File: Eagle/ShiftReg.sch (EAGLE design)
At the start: 194 parts, among them Q100 310mA/60V/1.6Ω, Q101 310mA/60V/1.6Ω, Q102 310mA/60V/1.6Ω, Q103 310mA/60V/1.6Ω, Q104 310mA/60V/1.6Ω, Q105 310mA/60V/1.6Ω, Q106 310mA/60V/1.6Ω, Q107 310mA/60V/1.6Ω, Q108 310mA/60V/1.6Ω, Q109 310mA/60V/1.6Ω, Q110 310mA/60V/1.6Ω, Q111 310mA/60V/1.6Ω, Q112 310mA/60V/1.6Ω, Q113 310mA/60V/1.6Ω, Q114 310mA/60V/1.6Ω, Q115 310mA/60V/1.6Ω, Q116 310mA/60V/1.6Ω, Q117 310mA/60V/1.6Ω, Q118 310mA/60V/1.6Ω, Q119 310mA/60V/1.6Ω, Q120 310mA/60V/1.6Ω, Q121 310mA/60V/1.6Ω, Q122 310mA/60V/1.6Ω, Q123 310mA/60V/1.6Ω, Q124 310mA/60V/1.6Ω, Q125 310mA/60V/1.6Ω, Q126 310mA/60V/1.6Ω, Q127 310mA/60V/1.6Ω, Q128 310mA/60V/1.6Ω, Q129 310mA/60V/1.6Ω, Q130 310mA/60V/1.6Ω, Q131 310mA/60V/1.6Ω, Q132 310mA/60V/1.6Ω, Q166 310mA/60V/1.6Ω, Q167 310mA/60V/1.6Ω, Q168 310mA/60V/1.6Ω, Q169 310mA/60V/1.6Ω, Q170 310mA/60V/1.6Ω, Q171 310mA/60V/1.6Ω, Q172 310mA/60V/1.6Ω, Q173 310mA/60V/1.6Ω, Q174 310mA/60V/1.6Ω, Q175 310mA/60V/1.6Ω, Q176 310mA/60V/1.6Ω, Q177 310mA/60V/1.6Ω, Q178 310mA/60V/1.6Ω, Q179 310mA/60V/1.6Ω, Q180 310mA/60V/1.6Ω, Q181 310mA/60V/1.6Ω, Q182 310mA/60V/1.6Ω, Q183 310mA/60V/1.6Ω, Q184 310mA/60V/1.6Ω, Q185 310mA/60V/1.6Ω, Q186 310mA/60V/1.6Ω, Q187 310mA/60V/1.6Ω, Q188 310mA/60V/1.6Ω, Q189 310mA/60V/1.6Ω, Q190 310mA/60V/1.6Ω, Q191 310mA/60V/1.6Ω, Q192 310mA/60V/1.6Ω, Q193 310mA/60V/1.6Ω, Q194 310mA/60V/1.6Ω, Q195 310mA/60V/1.6Ω, Q196 310mA/60V/1.6Ω, Q197 310mA/60V/1.6Ω, Q198 310mA/60V/1.6Ω, Q232 310mA/60V/1.6Ω, Q233 310mA/60V/1.6Ω, Q234 310mA/60V/1.6Ω, Q235 310mA/60V/1.6Ω, Q236 310mA/60V/1.6Ω, Q237 310mA/60V/1.6Ω, Q238 310mA/60V/1.6Ω, Q239 310mA/60V/1.6Ω, Q240 310mA/60V/1.6Ω, Q241 310mA/60V/1.6Ω, Q242 310mA/60V/1.6Ω, Q243 310mA/60V/1.6Ω, Q244 310mA/60V/1.6Ω, Q245 310mA/60V/1.6Ω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

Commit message: Rerouted for SOT23
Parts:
- removed Q166, Q167, Q168, Q169, Q170, Q171, Q172, Q173, Q174, Q175, Q176, Q177, Q178, Q179, Q180, Q181, Q182, Q183, Q184, Q185, Q186, Q187, Q188, Q189, Q190, Q191, Q192, Q193, Q194, Q195, Q196, Q197, Q198, Q232, Q233, Q234, Q235, Q236, Q237, Q238, Q239, Q240, Q241, Q242, Q243, Q244, Q245, Q246, Q247, Q248, Q249, Q250, Q251, Q252, Q253, Q254, Q255, Q256, Q257, Q258, Q259, Q260, Q261, Q262, Q263, Q264, Q42, Q43, Q44, Q45, Q46, Q47, Q48, Q49, Q58, Q59, Q60, Q61, Q62, Q63, Q64, Q65: 310mA/60V/1.6Ω, SparkFun-DiscreteSemi:MOSFET-NCH-2N7002PW
- removed R100, R101, R102, R103, R104, R105, R106, R107, R108, R109, R110, R111, R112, R19, R20, R21, R22, R27, R28, R71, R72, R73, R74, R75, R76, R77, R78, R79, R80, R81, R82, R83, R84, R99: (no value), SparkFun-Resistors:RESISTOR0805
- added LED1, LED2, LED3, LED4: (no value), led:LEDSQR2X5
- added Q1, Q2, Q3, Q4: (no value), XSNOR:NMOSREFLOW
- added Q10, Q11, Q12, Q13, Q133, Q134, Q135, Q136, Q137, Q138, Q139, Q14, Q140, Q141, Q142, Q143, Q144, Q145, Q146, Q147, Q148, Q149, Q15, Q150, Q151, Q152, Q153, Q154, Q155, Q156, Q157, Q158, Q159, Q16, Q160, Q161, Q162, Q163, Q164, Q165, Q25, Q26, Q27, Q28, Q29, Q30, Q31, Q32, Q67, Q68, Q69, Q70, Q71, Q72, Q73, Q74, Q75, Q76, Q77, Q78, Q79, Q80, Q81, Q82, Q83, Q84, Q85, Q86, Q87, Q88, Q89, Q9, Q90, Q91, Q92, Q93, Q94, Q95, Q96, Q97, Q98, Q99: 310mA/60V/1.6Ω, XSNOR:NMOSREFLOW
- added R1, R13, R14, R15, R16, R2, R3, R31, R32, R33, R34, R35, R36, R37, R38, R39, R4, R40, R41, R42, R5, R57, R58, R59, R6, R60, R61, R62, R63, R64, R65, R66, R67, R68, R69, R7, R70, R8: (no value), XSNOR:RESISTOR0805
- Q100, Q107, Q108, Q115, Q34, Q41: device SparkFun-DiscreteSemi:MOSFET-NCH-2N7002PW -> XSNOR:NMOSREFLOW; SPICEPREFIX M -> (none)
- Q101, Q102, Q103, Q104, Q105, Q106, Q109, Q110, Q111, Q112, Q113, Q114, Q116, Q118, Q119, Q120, Q121, Q122, Q123, Q126, Q127, Q128, Q129, Q130, Q131, Q36, Q37, Q38, Q39, Q40, Q52, Q53, Q54, Q55, Q56, Q57: device SparkFun-DiscreteSemi:MOSFET-NCH-2N7002PW -> XSNOR:NMOSREFLOW
- Q117, Q124, Q125, Q132, Q35, Q50, Q51, Q66: device SparkFun-DiscreteSemi:MOSFET-NCH-2N7002PW -> XSNOR:NMOSREFLOW; SPICEPREFIX (none) -> M
- R11, R12, R17, R18, R23, R24, R25, R26, R43, R44, R45, R46, R47, R48, R49, R50, R51, R52, R53, R54, R55, R56: device SparkFun-Resistors:RESISTOR0805 -> XSNOR:RESISTOR0805
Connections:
- removed net /Q0A1: Q36.G, Q39.D, Q40.D, Q46.G, R18.1
- removed net /Q0B: Q44.G, Q47.D, Q48.D, R22.1
- removed net /Q1A3: Q102.G, Q105.D, Q106.D, Q112.G, R46.1
- removed net /Q1B: Q110.G, Q113.D, Q114.D, R50.1
- removed net /Q2A5: Q168.G, Q171.D, Q172.D, Q178.G, R74.1
- removed net /Q2B: Q176.G, Q179.D, Q180.D, R78.1
- removed net /Q3A7: Q234.G, Q237.D, Q238.D, Q244.G, R102.1
- removed net /Q3B: Q242.G, Q245.D, Q246.D, R106.1
- removed net AUX1A': Q120.G, Q130.D, Q131.D, Q132.D, R56.2
- removed net LOAD1A': Q119.G, Q127.D, Q128.D, Q129.D, R55.2
- removed net N$116: Q243.D, Q244.D, Q245.G, R105.1
- removed net N$3: JP2.28
- removed net N$49: Q100.D, Q101.D, Q107.G, R43.1
- removed net N$50: Q103.D, Q104.D, Q105.G, R45.1
- removed net N$51: Q108.D, Q109.D, Q115.G, R47.1
- removed net N$52: Q111.D, Q112.D, Q113.G, R49.1
- removed net N$81: Q166.D, Q167.D, Q173.G, R71.1
- removed net N$82: Q169.D, Q170.D, Q171.G, R73.1
- removed net N$83: Q174.D, Q175.D, Q181.G, R75.1
- removed net N$84: Q177.D, Q178.D, Q179.G, R77.1
- removed net Q0A1: Q36.D, Q40.G, Q41.D, Q43.G, R12.1
- removed net Q1A3: Q102.D, Q106.G, Q107.D, Q109.G, R44.1
- removed net Q2A5: Q168.D, Q172.G, Q173.D, Q175.G, R72.1
- removed net Q3A7: Q234.D, Q238.G, Q239.D, Q241.G, R100.1
- removed net R0A: Q38.G, Q50.D, R23.2
- removed net S0A: Q35.G, Q50.G, Q51.D, Q52.D, Q53.D, Q54.D, R24.2
- new net AUX1A'-: Q71.G, Q81.D, Q82.D, Q83.D, R34.2
- new net LED+: JP2.28, LED1.A, LED2.A, LED3.A, LED4.A
- new net LOAD1A'-: Q70.G, Q78.D, Q79.D, Q80.D, R33.2
- new net N$10: Q92.D, Q93.D, Q99.G, R39.1
- new net N$100: Q119.D, Q123.G, Q124.D, Q126.G, R50.1
- new net N$101: Q119.G, Q122.D, Q123.D, Q129.G, R52.1
- new net N$102: Q127.G, Q130.D, Q131.D, R56.1
- new net N$103: Q86.G, Q89.D, Q90.D, Q96.G, R38.1
- new net N$104: Q86.D, Q90.G, Q91.D, Q93.G, R36.1
- new net N$105: Q94.G, Q97.D, Q98.D, R42.1
- new net N$11: Q95.D, Q96.D, Q97.G, R41.1
- new net N$110: Q53.G, Q56.D, Q57.D, R24.1
- new net N$111: Q37.G, Q40.D, Q41.D, Q55.G, R16.1
- new net N$112: Q37.D, Q41.G, Q50.D, Q52.G, R14.1
- new net N$12: Q150.D, Q151.D, Q157.G, R63.1
- new net N$13: Q153.D, Q154.D, Q155.G, R65.1
- new net N$14: Q158.D, Q159.D, Q165.G, R67.1
- new net N$15: Q161.D, Q162.D, Q163.G, R69.1
- new net N$16: Q117.D, Q118.D, Q124.G, R49.1
- new net N$17: Q120.D, Q121.D, Q122.G, R51.1
- new net N$18: Q125.D, Q126.D, Q132.G, R53.1
- new net N$19: Q128.D, Q129.D, Q130.G, R55.1
- new net N$2: Q38.D, Q39.D, Q40.G, R15.1
- new net N$20: Q3.D, R3.1
- new net N$21: Q4.D, R4.1
- new net N$22: LED4.C, R4.2
- new net N$23: LED3.C, R3.2
- new net N$24: LED2.C, R2.2
- new net N$25: LED1.C, R1.2
- new net N$7: Q54.D, Q55.D, Q56.G, R23.1
- new net N$8: Q84.D, Q85.D, Q91.G, R35.1
- new net N$9: Q87.D, Q88.D, Q89.G, R37.1
- new net R0A-: Q100.D, Q121.G, R43.2
- new net S0A-: Q100.G, Q101.D, Q102.D, Q103.D, Q104.D, Q118.G, R44.2
- net /CLK: now also Q117.G, Q120.G, Q150.G, Q153.G, Q35.G, Q38.G, Q84.G, Q87.G; no longer Q100.G, Q103.G, Q166.G, Q169.G, Q232.G, Q235.G, Q34.G, Q37.G
- net /OP1: now also Q112.G, Q115.G, Q145.G, Q148.G, Q29.G, Q32.G, Q79.G, Q82.G; no longer Q128.G, Q131.G, Q194.G, Q197.G, Q260.G, Q263.G, Q62.G, Q65.G
- net /OP2: now also Q108.G, Q114.G, Q141.G, Q147.G, Q25.G, Q31.G, Q75.G, Q81.G; no longer Q124.G, Q130.G, Q190.G, Q196.G, Q256.G, Q262.G, Q58.G, Q64.G
- net AUX0: now also Q116.G; no longer Q66.G
- net AUX0A': now also Q104.G, Q114.D, Q115.D, Q116.D, R48.2; no longer Q54.G, Q64.D, Q65.D, Q66.D, R28.2
- net AUX1: now also Q83.G; no longer Q132.G
- net AUX2: now also Q34.G; no longer Q198.G
- net AUX2A': now also Q13.G, Q31.D, Q32.D, Q34.D, R12.2; no longer Q186.G, Q196.D, Q197.D, Q198.D, R84.2
- net AUX3: now also Q149.G; no longer Q264.G
- net AUX3A': now also Q137.G, Q147.D, Q148.D, Q149.D, R62.2; no longer Q252.G, Q262.D, Q263.D, Q264.D, R112.2
- net CLK: now also Q125.G, Q128.G, Q158.G, Q161.G, Q51.G, Q54.G, Q92.G, Q95.G; no longer Q108.G, Q111.G, Q174.G, Q177.G, Q240.G, Q243.G, Q42.G, Q45.G
- net GND: now also Q1.S, Q10.S, Q11.S, Q12.S, Q13.S, Q133.S, Q134.S, Q135.S, Q136.S, Q137.S, Q138.S, Q139.S, Q14.S, Q140.S, Q141.S, Q142.S, Q143.S, Q144.S, Q145.S, Q146.S, Q147.S, Q148.S, Q149.S, Q15.S, Q150.S, Q151.S, Q152.S, Q153.S, Q154.S, Q155.S, Q156.S, Q157.S, Q158.S, Q159.S, Q16.S, Q160.S, Q161.S, Q162.S, Q163.S, Q164.S, Q165.S, Q2.S, Q25.S, Q26.S, Q27.S, Q28.S, Q29.S, Q3.S, Q30.S, Q31.S, Q32.S, Q4.S, Q67.S, Q68.S, Q69.S, Q70.S, Q71.S, Q72.S, Q73.S, Q74.S, Q75.S, Q76.S, Q77.S, Q78.S, Q79.S, Q80.S, Q81.S, Q82.S, Q83.S, Q84.S, Q85.S, Q86.S, Q87.S, Q88.S, Q89.S, Q9.S, Q90.S, Q91.S, Q92.S, Q93.S, Q94.S, Q95.S, Q96.S, Q97.S, Q98.S, Q99.S; no longer Q166.S, Q167.S, Q168.S, Q169.S, Q170.S, Q171.S, Q172.S, Q173.S, Q174.S, Q175.S, Q176.S, Q177.S, Q178.S, Q179.S, Q180.S, Q181.S, Q182.S, Q183.S, Q184.S, Q185.S, Q186.S, Q187.S, Q188.S, Q189.S, Q190.S, Q191.S, Q192.S, Q193.S, Q194.S, Q195.S, Q196.S, Q197.S, Q198.S, Q232.S, Q233.S, Q234.S, Q235.S, Q236.S, Q237.S, Q238.S, Q239.S, Q240.S, Q241.S, Q242.S, Q243.S, Q244.S, Q245.S, Q246.S, Q247.S, Q248.S, Q249.S, Q250.S, Q251.S, Q252.S, Q253.S, Q254.S, Q255.S, Q256.S, Q257.S, Q258.S, Q259.S, Q260.S, Q261.S, Q262.S, Q263.S, Q264.S, Q42.S, Q43.S, Q44.S, Q45.S, Q46.S, Q47.S, Q48.S, Q49.S, Q58.S, Q59.S, Q60.S, Q61.S, Q62.S, Q63.S, Q64.S, Q65.S
- net LOAD0: now also Q113.G; no longer Q63.G
- net LOAD0A': now also Q103.G, Q111.D, Q112.D, Q113.D, R47.2; no longer Q53.G, Q61.D, Q62.D, Q63.D, R27.2
- net LOAD1: now also Q80.G; no longer Q129.G
- net LOAD2: now also Q30.G; no longer Q195.G
- net LOAD2A': now also Q12.G, Q28.D, Q29.D, Q30.D, R11.2; no longer Q185.G, Q193.D, Q194.D, Q195.D, R83.2
- net LOAD3: now also Q146.G; no longer Q261.G
- net LOAD3A': now also Q136.G, Q144.D, Q145.D, Q146.D, R61.2; no longer Q251.G, Q259.D, Q260.D, Q261.D, R111.2
- net N$1: now also Q36.D, Q50.G, R13.1; no longer Q34.D, Q41.G, R11.1
- net N$113: now also Q160.G, Q163.D, Q164.D, R70.1; no longer Q232.D, Q233.D, Q239.G, R99.1
- net N$114: now also Q152.G, Q155.D, Q156.D, Q162.G, R66.1; no longer Q235.D, Q236.D, Q237.G, R101.1
- net N$115: now also Q152.D, Q156.G, Q157.D, Q159.G, R64.1; no longer Q240.D, Q241.D, Q247.G, R103.1
- net N$4: now also Q51.D, Q52.D, Q66.G; no longer Q37.D, Q38.D, Q39.G
- net N$5: now also Q1.D, R1.1; no longer Q42.D, Q43.D, Q49.G, R19.1
- net N$6: now also Q2.D, R2.1; no longer Q45.D, Q46.D, Q47.G, R21.1
- net NEXT0: now also Q110.G; no longer Q60.G
- net NEXT0A': now also Q102.G, Q108.D, Q109.D, Q110.D, R46.2; no longer Q52.G, Q58.D, Q59.D, Q60.D, R26.2
- net NEXT1: now also Q77.G; no longer Q126.G
- net NEXT1A': now also Q69.G, Q75.D, Q76.D, Q77.D, R32.2; no longer Q118.G, Q124.D, Q125.D, Q126.D, R54.2
- net NEXT2: now also Q27.G; no longer Q192.G
- net NEXT2A': now also Q11.G, Q25.D, Q26.D, Q27.D, R8.2; no longer Q184.G, Q190.D, Q191.D, Q192.D, R82.2
- net NEXT3: now also Q143.G; no longer Q258.G
- net NEXT3A': now also Q135.G, Q141.D, Q142.D, Q143.D, R60.2; no longer Q250.G, Q256.D, Q257.D, Q258.D, R110.2
- net OP1: now also Q106.G, Q109.G, Q139.G, Q142.G, Q15.G, Q26.G, Q73.G, Q76.G; no longer Q122.G, Q125.G, Q188.G, Q191.G, Q254.G, Q257.G, Q56.G, Q59.G
- net OP2: now also Q105.G, Q111.G, Q138.G, Q14.G, Q144.G, Q28.G, Q72.G, Q78.G; no longer Q121.G, Q127.G, Q187.G, Q193.G, Q253.G, Q259.G, Q55.G, Q61.G
- net OUT0: now also Q1.G, Q127.D, Q131.G, Q132.D, R54.1; no longer Q44.D, Q48.G, Q49.D, R20.1
- net OUT1: now also Q2.G, Q94.D, Q98.G, Q99.D, R40.1; no longer Q110.D, Q114.G, Q115.D, R48.1
- net OUT2: now also Q3.G, Q53.D, Q57.G, Q66.D, R18.1; no longer Q176.D, Q180.G, Q181.D, R76.1
- net OUT3: now also Q160.D, Q164.G, Q165.D, Q4.G, R68.1; no longer Q242.D, Q246.G, Q247.D, R104.1
- net PREV0: now also Q107.G; no longer Q57.G
- net PREV0A': now also Q101.G, Q105.D, Q106.D, Q107.D, R45.2; no longer Q51.G, Q55.D, Q56.D, Q57.D, R25.2
- net PREV1: now also Q74.G; no longer Q123.G
- net PREV1A': now also Q68.G, Q72.D, Q73.D, Q74.D, R31.2; no longer Q117.G, Q121.D, Q122.D, Q123.D, R53.2
- net PREV2: now also Q16.G; no longer Q189.G
- net PREV2A': now also Q10.G, Q14.D, Q15.D, Q16.D, R7.2; no longer Q183.G, Q187.D, Q188.D, Q189.D, R81.2
- net PREV3: now also Q140.G; no longer Q255.G
- net PREV3A': now also Q134.G, Q138.D, Q139.D, Q140.D, R59.2; no longer Q249.G, Q253.D, Q254.D, Q255.D, R109.2
- net R1A: now also Q67.D, Q88.G, R25.2; no longer Q104.G, Q116.D, R51.2
- net R2A: now also Q39.G, Q9.D, R5.2; no longer Q170.G, Q182.D, R79.2
- net R3A: now also Q133.D, Q154.G, R57.2; no longer Q236.G, Q248.D, R107.2
- net S1A: now also Q67.G, Q68.D, Q69.D, Q70.D, Q71.D, Q85.G, R26.2; no longer Q101.G, Q116.G, Q117.D, Q118.D, Q119.D, Q120.D, R52.2
- net S2A: now also Q10.D, Q11.D, Q12.D, Q13.D, Q36.G, Q9.G, R6.2; no longer Q167.G, Q182.G, Q183.D, Q184.D, Q185.D, Q186.D, R80.2
- net S3A: now also Q133.G, Q134.D, Q135.D, Q136.D, Q137.D, Q151.G, R58.2; no longer Q233.G, Q248.G, Q249.D, Q250.D, Q251.D, Q252.D, R108.2
- net VCC: now also R11.1, R12.1, R13.2, R14.2, R15.2, R16.2, R23.2, R24.2, R31.1, R32.1, R33.1, R34.1, R35.2, R36.2, R37.2, R38.2, R39.2, R40.2, R41.2, R42.2, R43.1, R44.1, R45.1, R46.1, R47.1, R48.1, R5.1, R51.2, R52.2, R53.2, R54.2, R55.2, R56.2, R57.1, R58.1, R59.1, R6.1, R60.1, R61.1, R62.1, R63.2, R64.2, R65.2, R66.2, R67.2, R68.2, R69.2, R7.1, R70.2, R8.1; no longer R100.2, R101.2, R102.2, R103.2, R104.2, R105.2, R106.2, R107.1, R108.1, R109.1, R11.2, R110.1, R111.1, R112.1, R12.2, R19.2, R20.2, R21.2, R22.2, R23.1, R24.1, R27.1, R28.1, R43.2, R44.2, R45.2, R46.2, R47.2, R48.2, R51.1, R52.1, R53.1, R54.1, R55.1, R56.1, R71.2, R72.2, R73.2, R74.2, R75.2, R76.2, R77.2, R78.2, R79.1, R80.1, R81.1, R82.1, R83.1, R84.1, R99.2
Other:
- moved on the sheet: R11, R12, R17, R18, R23, R24, R25, R26, R43, R44, R45, R46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

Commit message: Cleanups of PCBs
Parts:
- JP2: device pinhead:PINHD-1X30 -> XSNOR:PINHD-1X30
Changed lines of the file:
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@@
 </classes>
 <parts>
-<part name="JP2" library="pinhead" library_urn="urn:adsk.eagle:library:325" deviceset="PINHD-1X30" device="" package3d_urn="urn:adsk.eagle:package:22460/2"/>
+<part name="JP2" library="XSNOR" library_urn="urn:adsk.eagle:library:1320997" deviceset="PINHD-1X30" device="" package3d_urn="urn:adsk.eagle:package:1346145/1"/>
 <part name="GND1" library="supply1" library_urn="urn:adsk.eagle:library:371" deviceset="GND" device=""/>
 <part name="P+1" library="supply1" library_urn="urn:adsk.eagle:library:371" deviceset="VCC" device=""/>

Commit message: Added clear to ShiftReg
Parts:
- added Q17, Q18, Q19, Q20, Q5, Q6, Q7, Q8: 310mA/60V/1.6Ω, XSNOR:NMOSREFLOW
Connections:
- new net CLR: JP2.7, Q17.G, Q18.G, Q19.G, Q20.G, Q5.G, Q6.G, Q7.G, Q8.G
- net GND: now also Q17.S, Q18.S, Q19.S, Q20.S, Q5.S, Q6.S, Q7.S, Q8.S
- net N$100: now also Q5.D
- net N$104: now also Q8.D
- net N$112: now also Q19.D
- net N$115: now also Q18.D
- net OUT0: now also Q6.D
- net OUT1: now also Q7.D
- net OUT2: now also Q20.D
- net OUT3: now also Q17.D
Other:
- moved on the sheet: Q125, Q126, Q127, Q128, Q129, Q130, Q131, Q132, Q158, Q159, Q160, Q161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

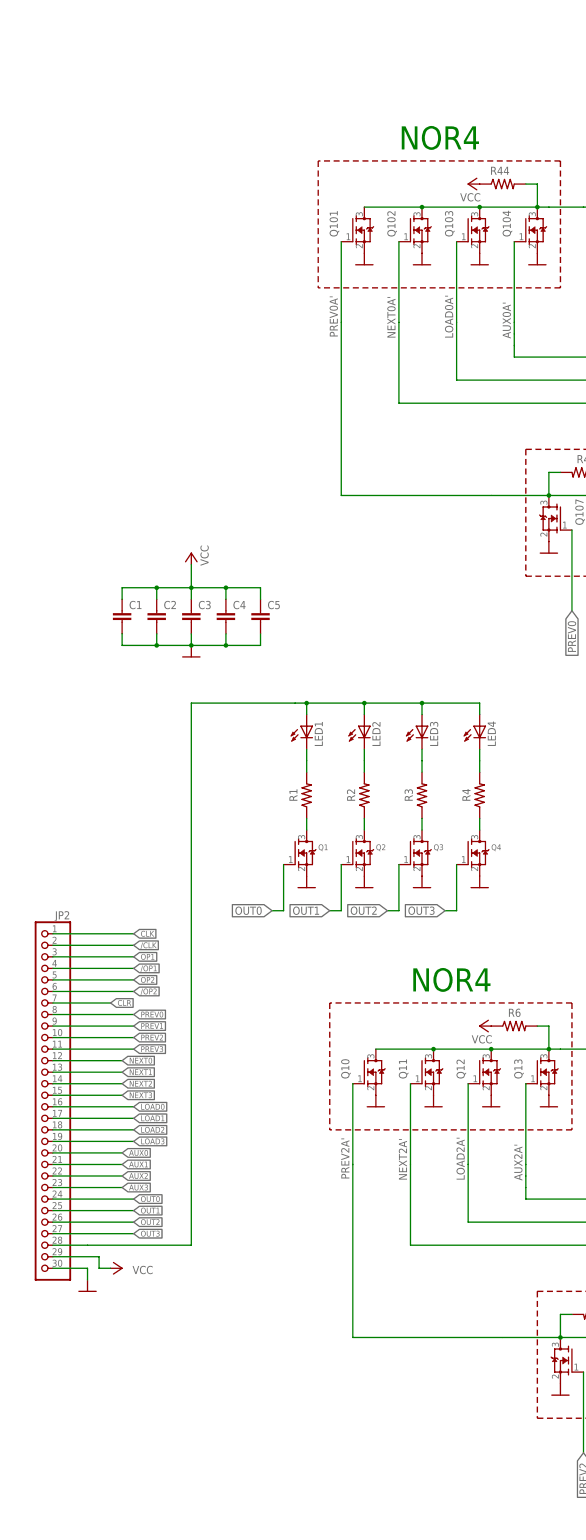
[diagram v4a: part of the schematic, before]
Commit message: Shiftreg pcb have its own inverters for control signals
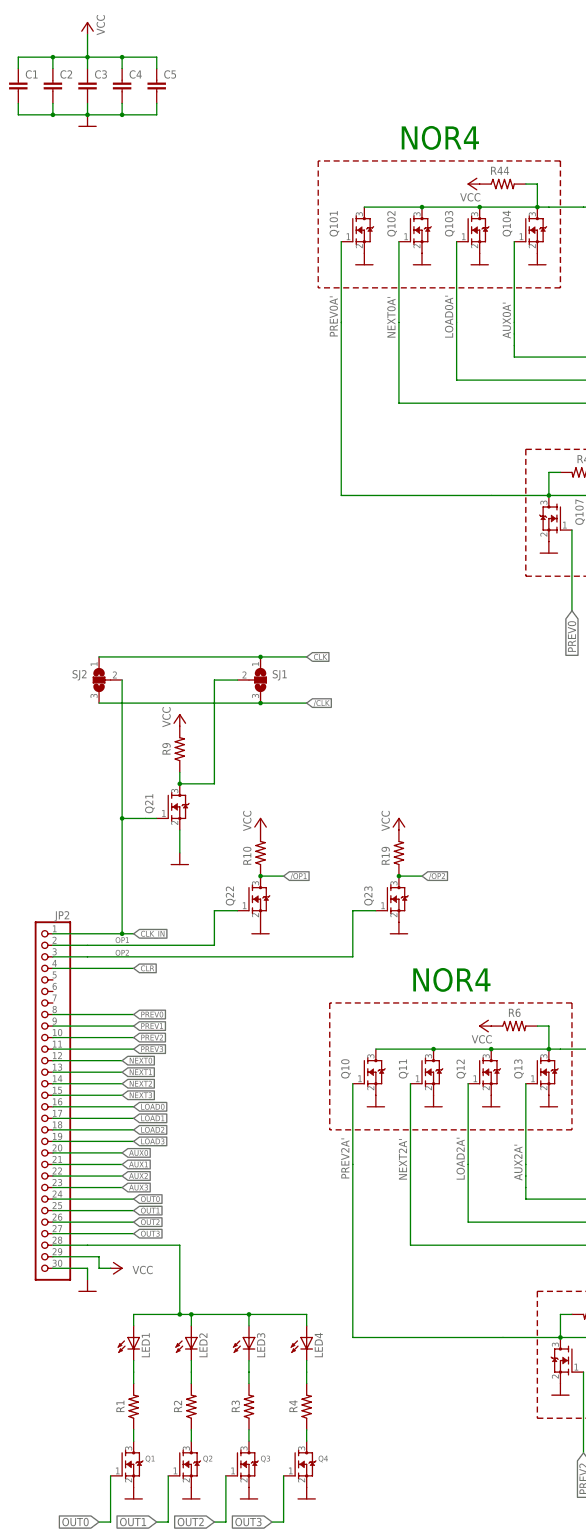
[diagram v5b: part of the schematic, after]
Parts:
- added Q21, Q22, Q23: 310mA/60V/1.6Ω, XSNOR:NMOSREFLOW
- added R10, R19, R9: (no value), XSNOR:RESISTOR0805
- added SJ1, SJ2: (no value), jumper:SJ2W
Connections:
- new net CLK_IN: JP2.1, Q21.G, SJ2.2
- new net N$3: Q21.D, R9.1, SJ1.2
- net /CLK: now also SJ1.3, SJ2.3; no longer JP2.2
- net /OP1: now also Q22.D, R10.1; no longer JP2.4
- net /OP2: now also Q23.D, R19.1; no longer JP2.6
- net CLK: now also SJ1.1, SJ2.1; no longer JP2.1
- net CLR: now also JP2.4; no longer JP2.7
- net GND: now also Q21.S, Q22.S, Q23.S
- net OP1: now also JP2.2, Q22.G; no longer JP2.3
- net OP2: now also JP2.3, Q23.G; no longer JP2.5
- net VCC: now also R10.2, R19.2, R9.2
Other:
- moved on the sheet: C1, C2, C3, C4, C5, LED1, LED2, LED3, LED4, Q1, Q2, Q3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
